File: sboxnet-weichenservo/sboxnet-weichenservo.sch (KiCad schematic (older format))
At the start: 33 parts, among them J1 Screw_Terminal_01x02, J10 Conn_01x03_Male, J11 Conn_01x03_Male, J12 Conn_01x03_Male, J2 Screw_Terminal_01x04, J3 Conn_02x17_Odd_Even, J4 Screw_Terminal_01x04, J5 Conn_01x03_Male, J6 Conn_01x03_Male, J7 Conn_01x03_Male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

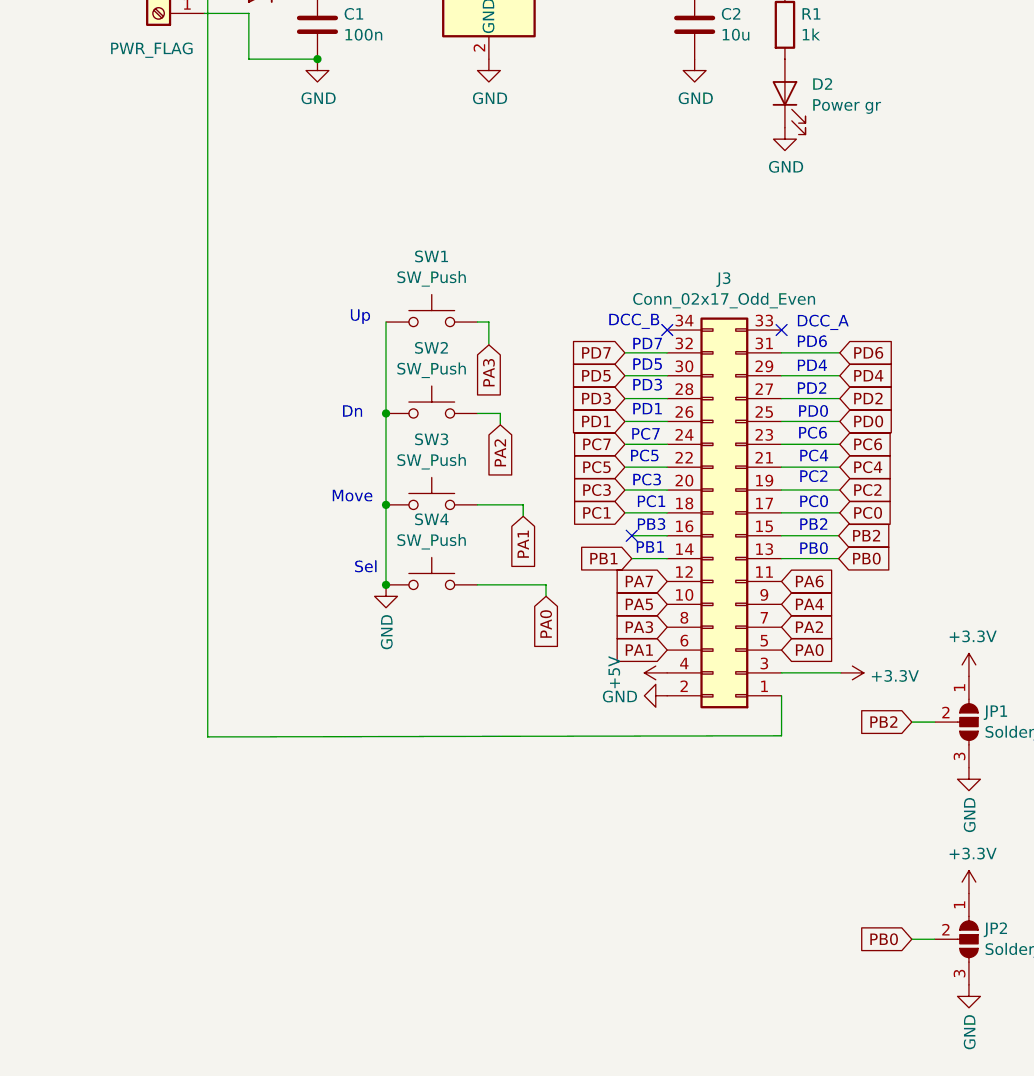
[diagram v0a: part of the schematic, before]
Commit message: added weichen-servo-ctrl
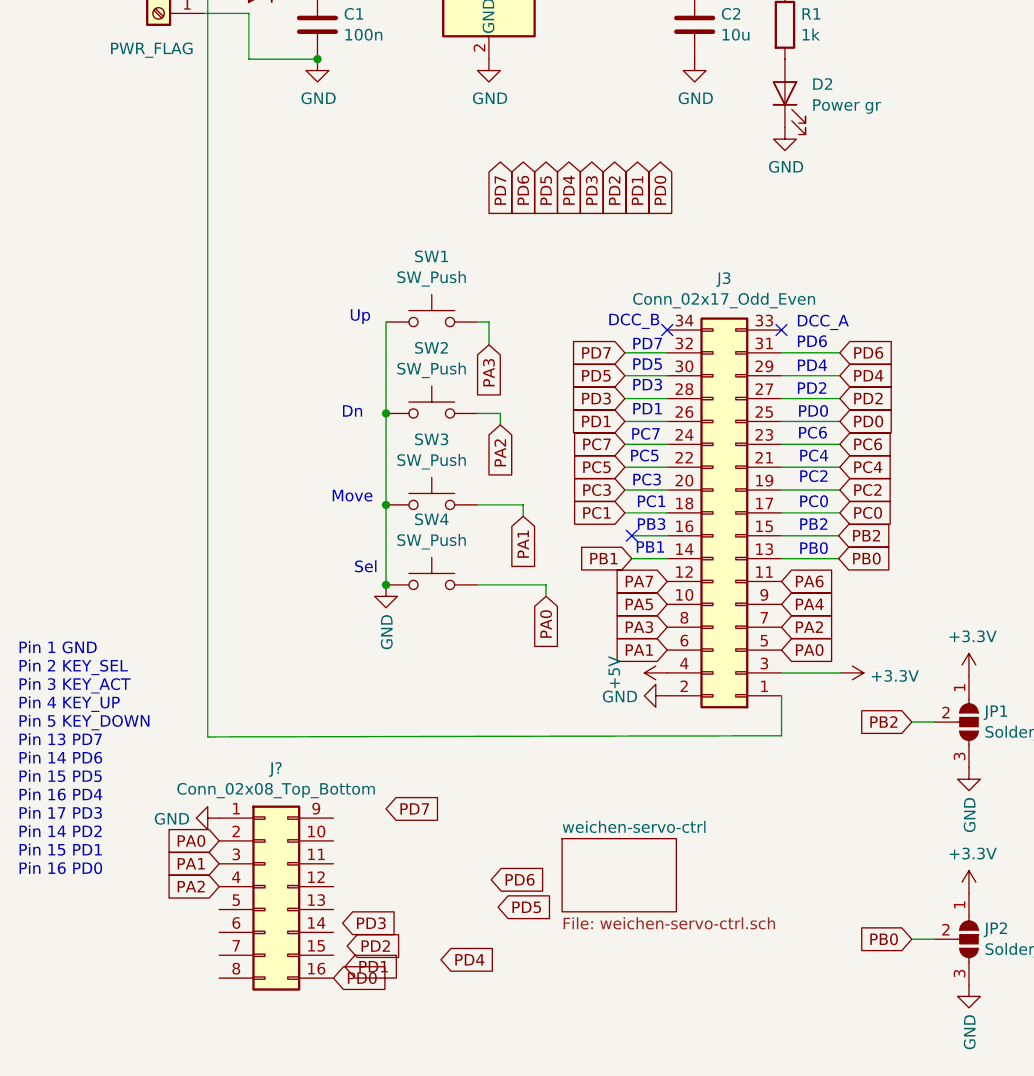
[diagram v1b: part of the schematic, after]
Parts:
- added J?: Conn_02x08_Top_Bottom, symbol Connector_Generic:Conn_02x08_Top_Bottom
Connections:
- net GND: now also J?.1 (Pin_1)
- net PA0: now also J?.2 (Pin_2)
- net PA1: now also J?.3 (Pin_3)
- net PA2: now also J?.4 (Pin_4)
- net PD0: now also J?.16 (Pin_16)
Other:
- note added: "Pin 1 GND\nPin 2 KEY_SEL\nPin 3 KEY_ACT\nPin 4 KEY_UP\nPin 5 KEY_DOWN\nPin 13 PD7\nPin 14 PD6\nPin 15 PD5\nPin 16 PD4\nPin 17 PD3\nPin 14 PD2\nPin 15 PD1\nPin 16 PD0"
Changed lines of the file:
@@
 $Descr A4 11693 8268
 encoding utf-8
-Sheet 1 1
+Sheet 1 2
 Title "sboxnet weichenservo"
 Date "31.08.2019"
@@
 	1    0    0    -1
 $EndComp
-Text GLabel 4200 2600 3    50   Input ~ 0
-PD7
-Text GLabel 4300 2600 3    50   Input ~ 0
-PD6
-Text GLabel 4400 2600 3    50   Input ~ 0
-PD5
-Text GLabel 4500 2600 3    50   Input ~ 0
-PD4
-Text GLabel 4600 2600 3    50   Input ~ 0
-PD3
-Text GLabel 4700 2600 3    50   Input ~ 0
-PD2
-Text GLabel 4800 2600 3    50   Input ~ 0
-PD1
-Text GLabel 4900 2600 3    50   Input ~ 0
-PD0
 Text GLabel 4230 5735 2    50   Input ~ 0
 PA4
@@
 	0    1    1    0
 $EndComp
+Text GLabel 4900 2600 3    50   Input ~ 0
+PD0
+Text GLabel 4800 2600 3    50   Input ~ 0
+PD1
+Text GLabel 4700 2600 3    50   Input ~ 0
+PD2
+Text GLabel 4600 2600 3    50   Input ~ 0
+PD3
+Text GLabel 4500 2600 3    50   Input ~ 0
+PD4
+Text GLabel 4400 2600 3    50   Input ~ 0
+PD5
+Text GLabel 4300 2600 3    50   Input ~ 0
+PD6
+Text GLabel 4200 2600 3    50   Input ~ 0
+PD7
+Text GLabel 3700 3800 3    50   Input ~ 0
+PD0
+Text GLabel 3600 3800 3    50   Input ~ 0
+PD1
+Text GLabel 3500 3800 3    50   Input ~ 0
+PD2
+Text GLabel 3400 3800 3    50   Input ~ 0
+PD3
+Text GLabel 3300 3800 3    50   Input ~ 0
+PD4
+Text GLabel 3200 3800 3    50   Input ~ 0
+PD5
+Text GLabel 3100 3800 3    50   Input ~ 0
+PD6
+Text GLabel 3000 3800 3    50   Input ~ 0
+PD7
+$Sheet
+S 3270 6760 500  320
+U 61281C62
+F0 "weichen-servo-ctrl" 50
+F1 "weichen-servo-ctrl.sch" 50
+$EndSheet
+Text Notes 890  6930 0    50   ~ 0
+Pin 1 GND\nPin 2 KEY_SEL\nPin 3 KEY_ACT\nPin 4 KEY_UP\nPin 5 KEY_DOWN\nPin 13 PD7\nPin 14 PD6\nPin 15 PD5\nPin 16 PD4\nPin 17 PD3\nPin 14 PD2\nPin 15 PD1\nPin 16 PD0
+Text GLabel 2270 7370 2    50   Input ~ 0
+PD0
+Text GLabel 2320 7320 2    50   Input ~ 0
+PD1
+Text GLabel 2330 7230 2    50   Input ~ 0
+PD2
+Text GLabel 2310 7130 2    50   Input ~ 0
+PD3
+Text GLabel 2740 7290 2    50   Input ~ 0
+PD4
+Text GLabel 2990 7060 2    50   Input ~ 0
+PD5
+Text GLabel 2960 6940 2    50   Input ~ 0
+PD6
+Text GLabel 2500 6630 2    50   Input ~ 0
+PD7
+$Comp
+L power:GND #PWR?
+U 1 1 612C5102
+P 1770 6670
+F 0 "#PWR?" H 1770 6420 50  0001 C CNN
+F 1 "GND" V 1775 6542 50  0000 R CNN
+F 2 "" H 1770 6670 50  0001 C CNN
+F 3 "" H 1770 6670 50  0001 C CNN
+	1    1770 6670
+	0    1    1    0
+$EndComp
+Text GLabel 1770 6770 0    50   Input ~ 0
+PA0
+Text GLabel 1770 6870 0    50   Input ~ 0
+PA1
+Text GLabel 1770 6970 0    50   Input ~ 0
+PA2
+$Comp
+L Connector_Generic:Conn_02x08_Top_Bottom J?
+U 1 1 612D070E
+P 1970 6970
+F 0 "J?" H 2020 7487 50  0000 C CNN
+F 1 "Conn_02x08_Top_Bottom" H 2020 7396 50  0000 C CNN
+F 2 "" H 1970 6970 50  0001 C CNN
+F 3 "~" H 1970 6970 50  0001 C CNN
+	1    1970 6970
+	1    0    0    -1
+$EndComp
 $EndSCHEMATC

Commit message: mit weichen-servo-ctrl
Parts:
- D3: value D_Schottky -> BAT 54J NXP; footprint (none) -> Diode_SMD:D_SOD-323F
- J13: renamed from J?; footprint (none) -> Connector_PinSocket_2.54mm:PinSocket_2x10_P2.54mm_Vertical
- RN1: renamed from RN?; value R_Network15 -> 4816P-T02-471LF 15x470; footprint (none) -> Package_SO:SOIC-16W_5.3x10.2mm_P1.27mm
- RN2: renamed from RN?; value R_Network13 -> 4816P-2-103 13x 10k; footprint Resistor_THT:R_Array_SIP14 -> Package_SO:SOIC-14W_7.5x9mm_P1.27mm
- RN3: footprint Package_SO:SOIC-14W_7.5x9mm_P1.27mm -> Package_SO:SOIC-16W-12_7.5x10.3mm_P1.27mm
- U2: footprint Package_SO:SOIC-20W_7.5x12.8mm_P1.27mm -> Package_SO:TSSOP-20_4.4x6.5mm_P0.65mm
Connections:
- net VCC is gone; now on net +5V: U3.16 (VCC)
- net PA3: now also J13.5 (Pin_5)
- net PD1: now also J13.15 (Pin_15)
- net PD2: now also J13.14 (Pin_14)
- net PD3: now also J13.13 (Pin_13)
- net PD4: now also J13.12 (Pin_12)
- net PD5: now also J13.11 (Pin_11)
- net PD6: now also J13.10 (Pin_10)
- net PD7: now also J13.9 (Pin_9)
- no-connect marks 16 -> 32
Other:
- note added: "Pin 1 GND\nPin 2 KEY_SEL\nPin 3 KEY_ACT\nPin 4 KEY_UP\nPin 5 KEY_DOWN\nPin 9 PD7\nPin 10 PD6\nPin 11 PD5\nPin 12 PD4\nPin 13 PD3\nPin 14 PD2\nPin 15 PD1\nPin 16 PD0"
- note removed: "PB0"
- note removed: "PB1"
- note removed: "PB2"
- note removed: "PB3"
- note removed: "PC0"
- note removed: "PC1"
- note removed: "PC2"
- note removed: "PC3"
- note removed: "PC4"
- note removed: "PC5"
- note removed: "PC6"
- note removed: "PC7"
- note removed: "PD0"
- note removed: "PD1"
- note removed: "PD2"
- note removed: "PD3"
- note removed: "PD4"
- note removed: "PD5"
- note removed: "PD6"
- note removed: "PD7"
- note removed: "Pin 1 GND\nPin 2 KEY_SEL\nPin 3 KEY_ACT\nPin 4 KEY_UP\nPin 5 KEY_DOWN\nPin 13 PD7\nPin 14 PD6\nPin 15 PD5\nPin 16 PD4\nPin 17 PD3\nPin 14 PD2\nPin 15 PD1\nPin 16 PD0"
- moved on the sheet: J13, J3

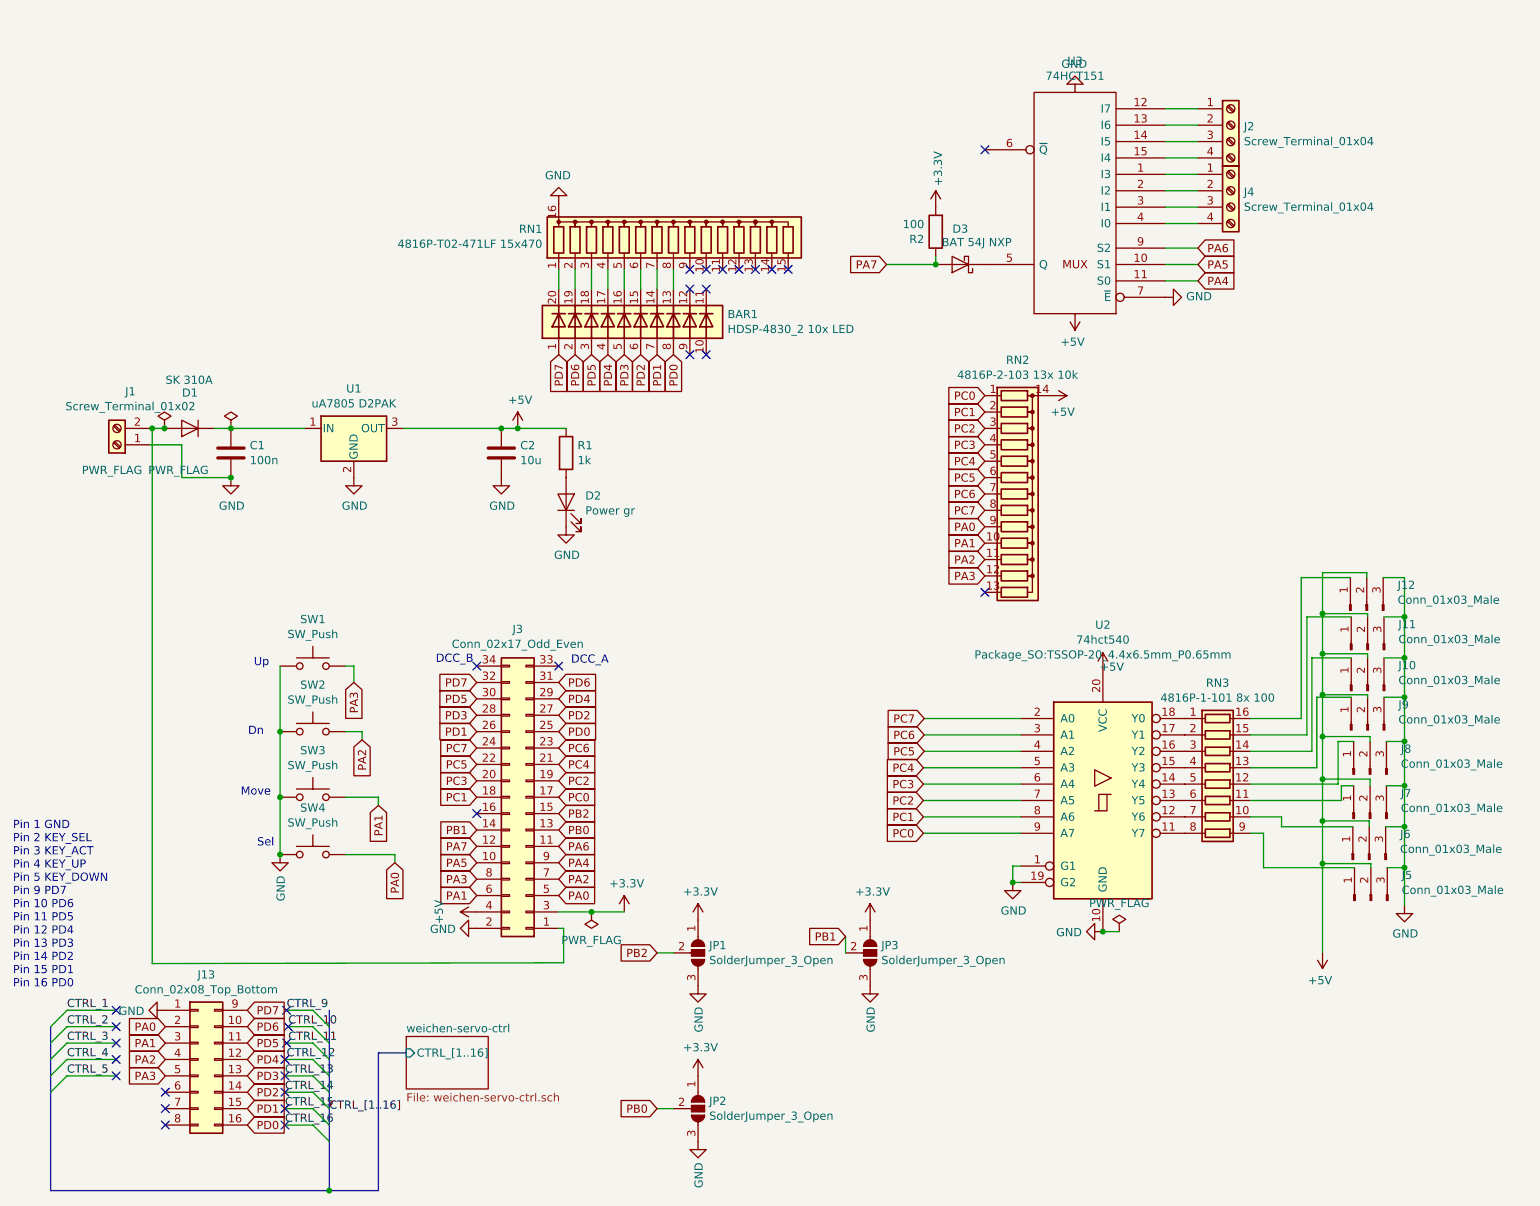
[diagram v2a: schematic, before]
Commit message: weichenservo mit Modulkennung
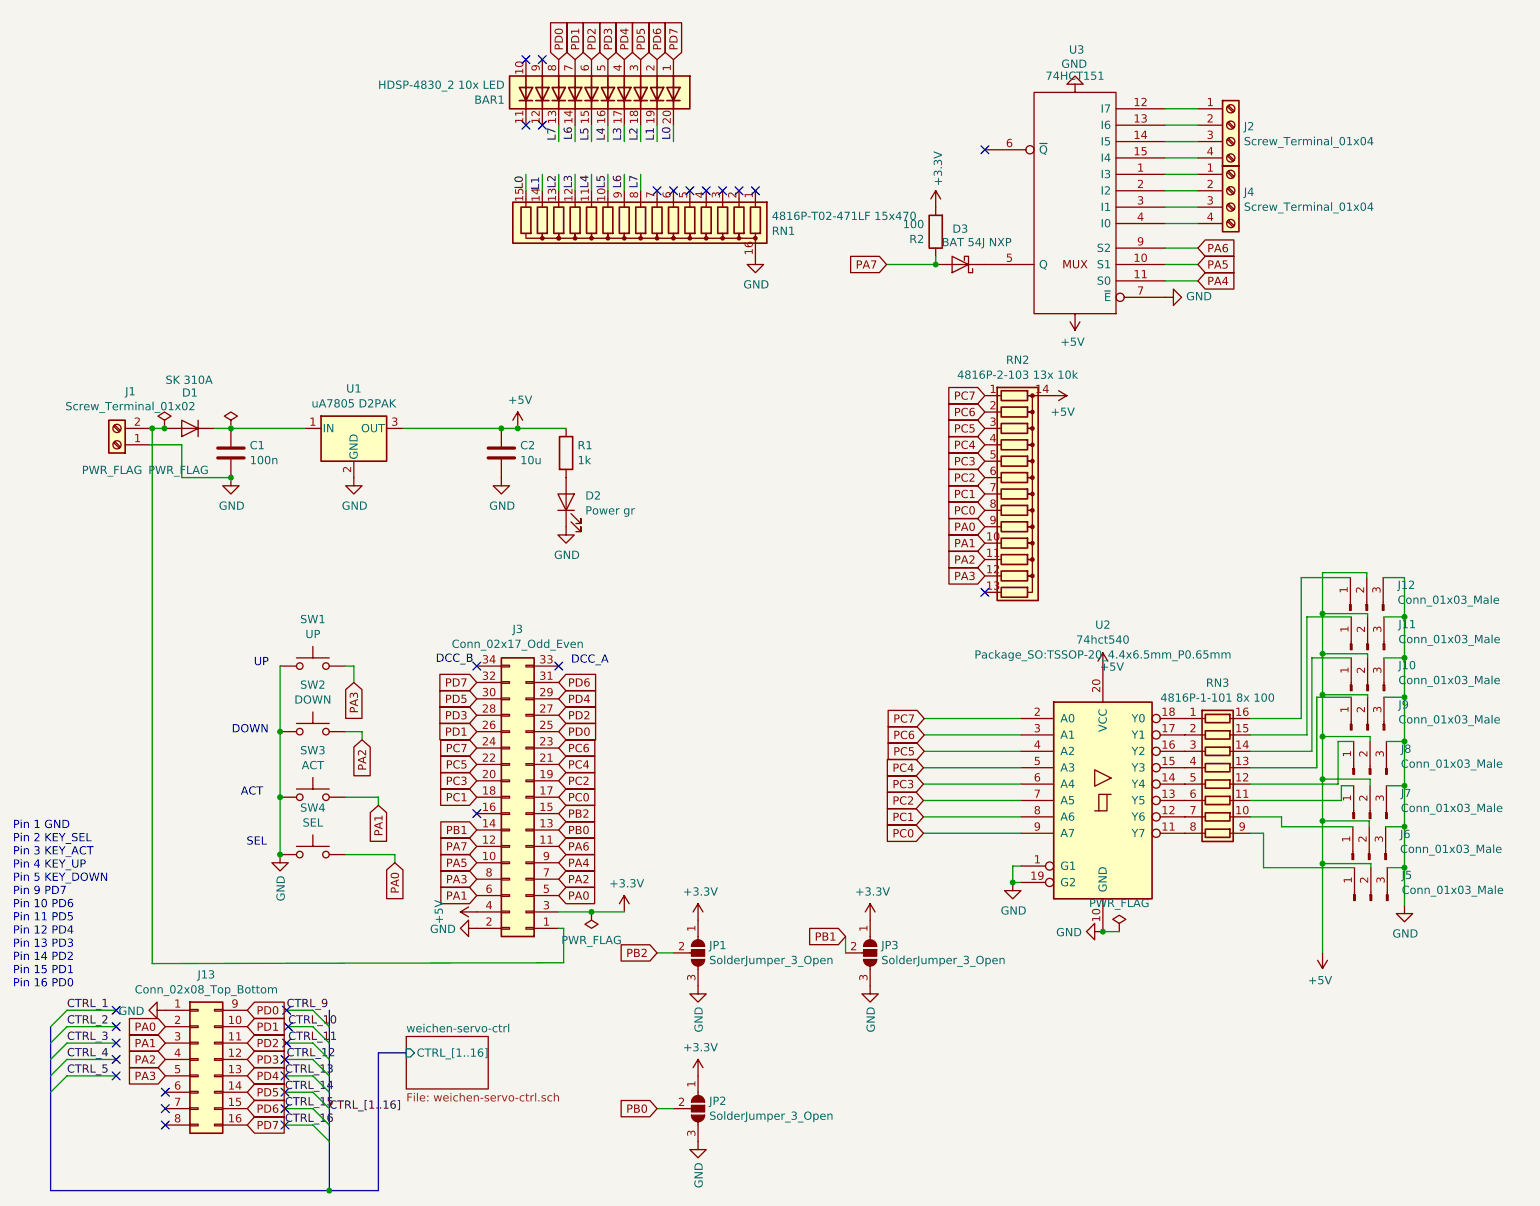
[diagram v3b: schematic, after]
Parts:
- J13: footprint Connector_PinSocket_2.54mm:PinSocket_2x10_P2.54mm_Vertical -> Connector_PinSocket_2.54mm:PinSocket_2x08_P2.54mm_Vertical
- RN2: footprint Package_SO:SOIC-14W_7.5x9mm_P1.27mm -> sboxnet:soic-14-8-6
- RN3: footprint Package_SO:SOIC-16W-12_7.5x10.3mm_P1.27mm -> Package_SO:SOIC-16W_5.3x10.2mm_P1.27mm
- SW1: value SW_Push -> UP
- SW2: value SW_Push -> DOWN
- SW3: value SW_Push -> ACT
- SW4: value SW_Push -> SEL
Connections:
- net labels added: L0, L1, L2, L3, L4, L5, L6, L7
- wire segments 141 -> 149
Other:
- note added: "ACT"
- note added: "DOWN"
- note added: "SEL"
- note added: "UP"
- note removed: "Dn"
- note removed: "Move"
- note removed: "Sel"
- note removed: "Up"
- moved on the sheet: BAR1, RN1
